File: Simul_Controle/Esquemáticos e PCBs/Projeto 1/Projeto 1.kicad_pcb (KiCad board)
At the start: 2 copper layers, 50 x 50 mm, 11 parts, among them J1 Conn_01x03_Pin, J2 Conn_01x02, J3 Conn_01x02, U2 LF355

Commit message: Fixed errors on board inspection and brought RV1 closer to opamp in hopes of minimizing noise, probably wont help much
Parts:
- moved RV1 1.20 mm to (38.3, 47.6)
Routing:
- net Vout: track 56.0 -> 52.8 mm
- net B1: track 5.94 -> 4.66 mm

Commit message: Pre last resort filter, still has an annoying high pitched noise in, but that should be gone with the 2 kHz filter that will be applied later
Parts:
- moved C4 1.29 mm to (35.8, 69.6), turned to 90 degrees
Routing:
- net Vee: track 20.5 -> 19.9 mm

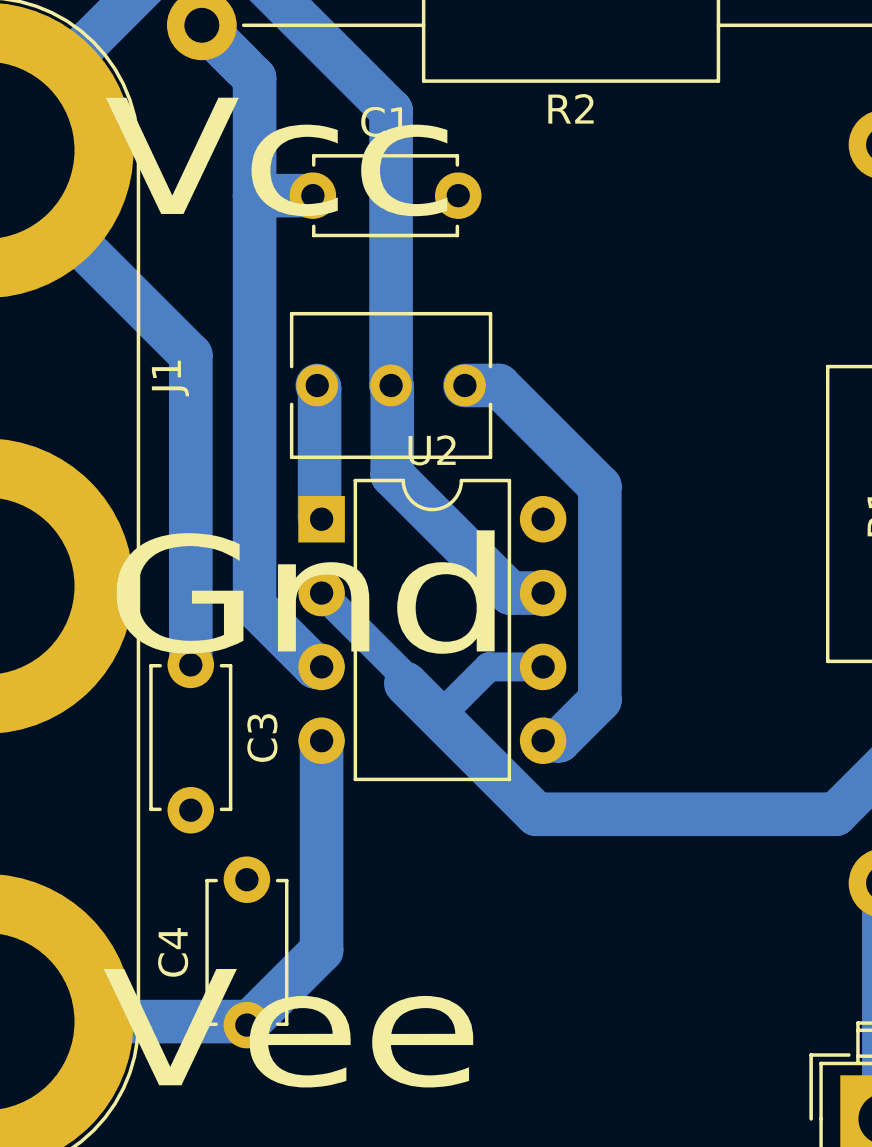
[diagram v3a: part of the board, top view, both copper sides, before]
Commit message: Fixed typo on LF356 (previously 336) and added simulation for LF351, which was the closest available IC
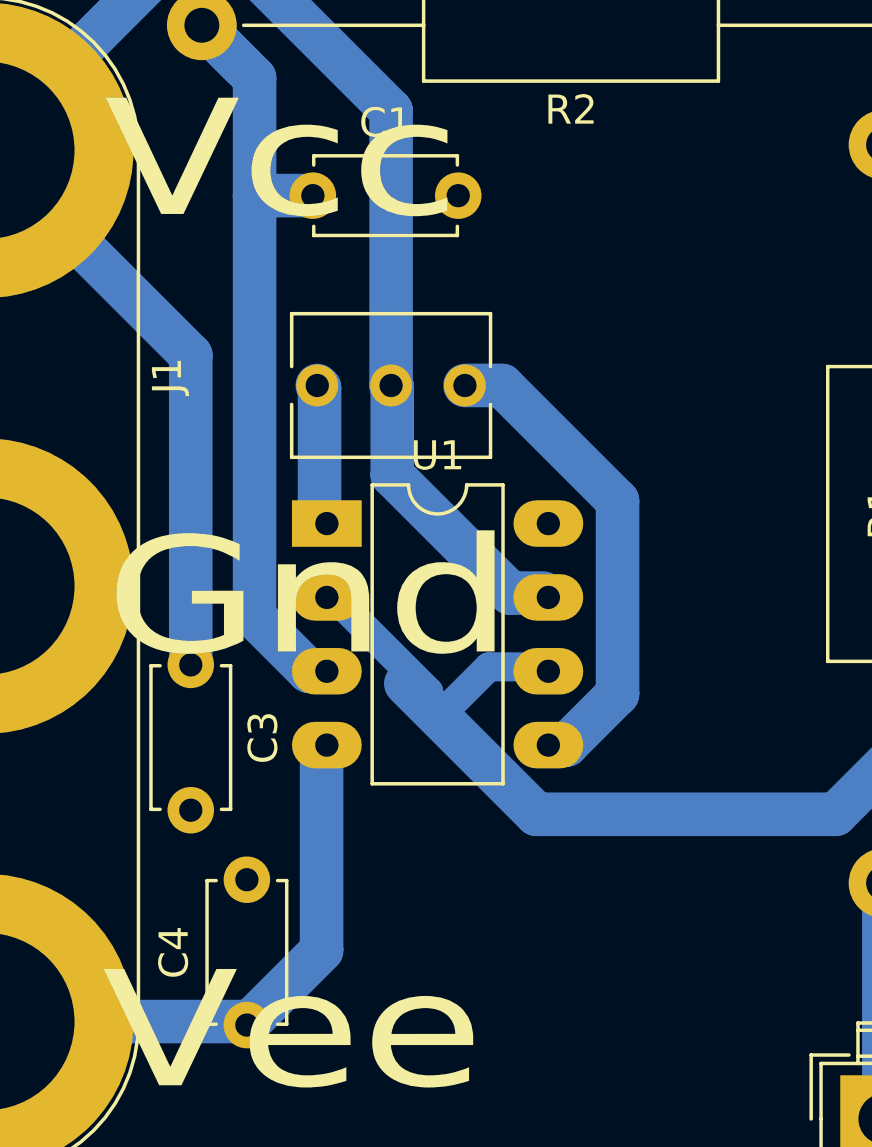
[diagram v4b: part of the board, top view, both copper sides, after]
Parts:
- removed U2: LF355, Package_DIP:DIP-8_W7.62mm
- added U1: LF355, Package_DIP:DIP-8_W7.62mm_LongPads, F.Cu at (38.6, 52.3)
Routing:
- net B5: track 16.0 -> 16.6 mm

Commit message: Adicionado conversor flyback
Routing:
- net Vout: track 52.7 -> 54.9 mm
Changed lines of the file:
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@@
   (segment (start 59.69 37.34) (end 57.76 39.27) (width 1.5) (layer "B.Cu") (net 2))
   (segment (start 66.14 35.18) (end 66.16 35.2) (width 1.5) (layer "B.Cu") (net 2))
-  (segment (start 42.09 58.095837) (end 42.09 58.39) (width 1) (layer "B.Cu") (net 3))
+  (segment (start 41.305 57.310837) (end 41.305 57.822717) (width 1) (layer "B.Cu") (net 3))
   (segment (start 66.54 51.87) (end 66.54 40.58) (width 1.5) (layer "B.Cu") (net 3))
+  (segment (start 46.03 57.25) (end 44.16 57.25) (width 1) (layer "B.Cu") (net 3))
+  (segment (start 41.727717 57.4) (end 41.305 57.822717) (width 1) (layer "B.Cu") (net 3))
+  (segment (start 66.54 40.58) (end 66.16 40.2) (width 1.5) (layer "B.Cu") (net 3))
+  (segment (start 41.305 58.535) (end 41.305 57.822717) (width 1.5) (layer "B.Cu") (net 3))
+  (segment (start 46.21 57.4) (end 41.727717 57.4) (width 1) (layer "B.Cu") (net 3))
+  (segment (start 45.09 62.32) (end 41.305 58.535) (width 1.5) (layer "B.Cu") (net 3))
+  (segment (start 38.854163 54.86) (end 41.305 57.310837) (width 1) (layer "B.Cu") (net 3))
+  (segment (start 56.09 62.32) (end 45.09 62.32) (width 1.5) (layer "B.Cu") (net 3))
+  (segment (start 38.59 54.86) (end 38.854163 54.86) (width 1) (layer "B.Cu") (net 3))
   (segment (start 66.54 51.87) (end 56.09 62.32) (width 1.5) (layer "B.Cu") (net 3))
-  (segment (start 38.59 54.86) (end 38.854163 54.86) (width 1) (layer "B.Cu") (net 3))
-  (segment (start 46.03 57.25) (end 44.16 57.25) (width 1) (layer "B.Cu") (net 3))
-  (segment (start 56.09 62.32) (end 45.802283 62.32) (width 1.5) (layer "B.Cu") (net 3))
-  (segment (start 45.802283 62.32) (end 41.305 57.822717) (width 1.5) (layer "B.Cu") (net 3))
-  (segment (start 66.54 40.58) (end 66.16 40.2) (width 1.5) (layer "B.Cu") (net 3))
-  (segment (start 44.16 57.25) (end 42.446141 58.963859) (width 1) (layer "B.Cu") (net 3))
-  (segment (start 38.854163 54.86) (end 42.09 58.095837) (width 1) (layer "B.Cu") (net 3))
   (segment (start 40.84 50.65137) (end 44.89863 54.71) (width 1.5) (layer "B.Cu") (net 4))
   (segment (start 40.8 47.57) (end 40.84 47.61) (width 1.5) (layer "B.Cu") (net 4))
